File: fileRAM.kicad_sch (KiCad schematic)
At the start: 13 parts

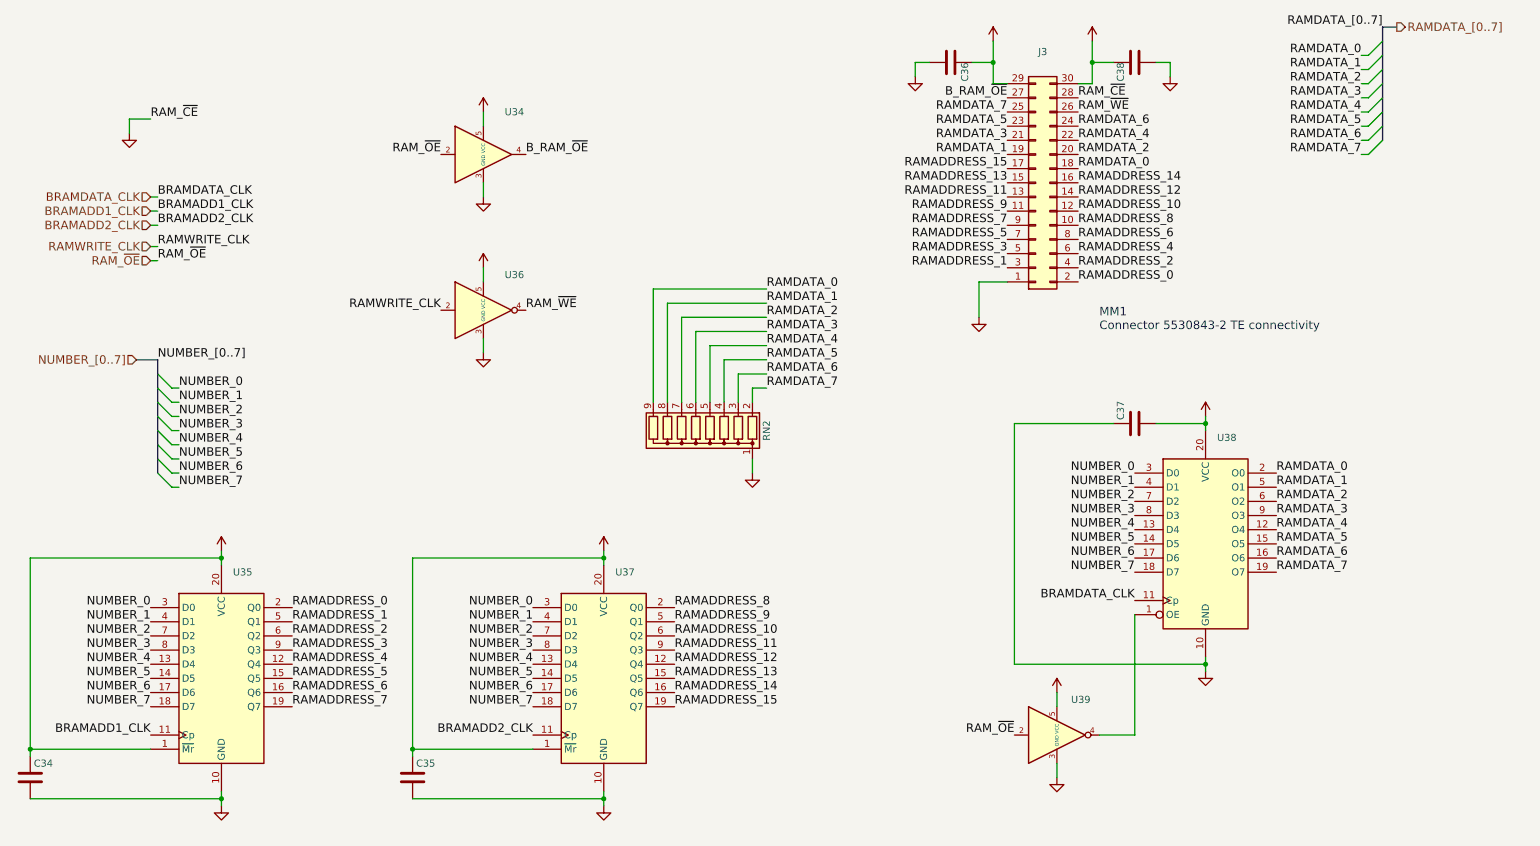
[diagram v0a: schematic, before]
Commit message: Updating descriptions
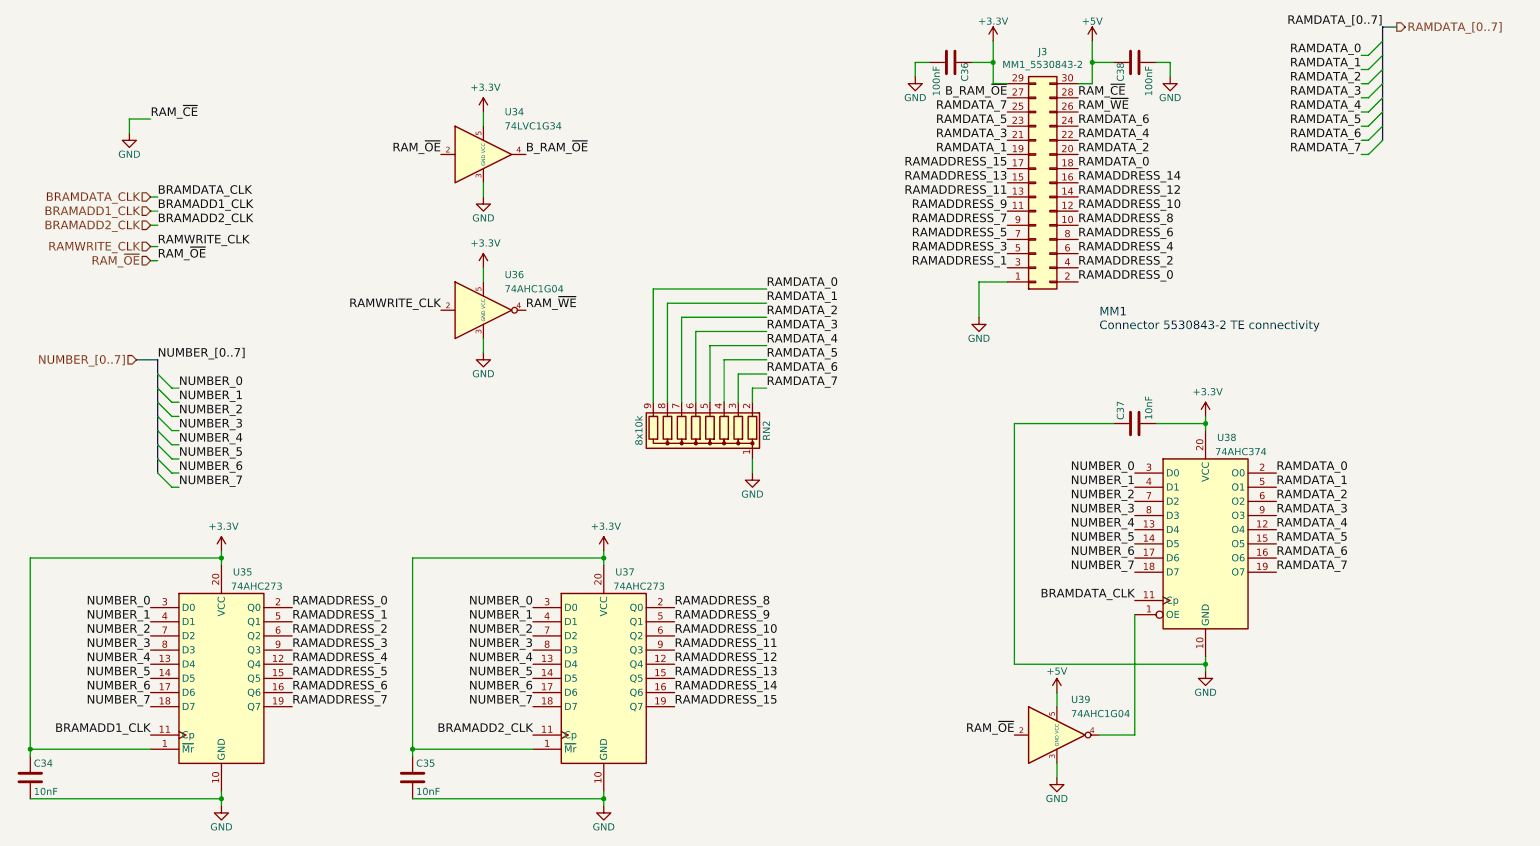
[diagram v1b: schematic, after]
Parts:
- C34, C35, C37: value (none) -> 10nF; footprint (none) -> Capacitor_SMD:C_0805_2012Metric
- C36, C38: value (none) -> 100nF; footprint (none) -> Capacitor_SMD:C_0805_2012Metric
- J3: value (none) -> MM1_5530843-2; footprint (none) -> TE5530843-2:TE_5530843-2
- RN2: value (none) -> 8x10k; footprint (none) -> Resistor_THT:R_Array_SIP9
- U34: value (none) -> 74LVC1G34; footprint (none) -> Package_TO_SOT_SMD:SOT-23-5
- U35, U37: value (none) -> 74AHC273; footprint (none) -> Package_SO:SOIC-20W_7.5x12.8mm_P1.27mm
- U36, U39: value (none) -> 74AHC1G04; footprint (none) -> Package_TO_SOT_SMD:SOT-23-5
- U38: value (none) -> 74AHC374; footprint (none) -> Package_SO:SOIC-20W_7.5x12.8mm_P1.27mm

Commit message: Finally remove clock sync, big improvement for the "if" instruction check (faster tps, less gates)
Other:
- note added: "RAM_~{CE}"
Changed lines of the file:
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@@
   (junction (at 16.51 151.13) (diameter 0) (color 0 0 0 0)
   )
+  (junction (at 220.98 34.29) (diameter 0) (color 0 0 0 0)
+  )
   (junction (at 207.01 27.94) (diameter 0) (color 0 0 0 0)
   )
@@
     (stroke (width 0) (type default) (color 0 0 0 0))
   )
-  (wire (pts (xy 38.1 38.1) (xy 34.29 38.1))
-    (stroke (width 0) (type default) (color 0 0 0 0))
-  )
   (bus (pts (xy 39.37 91.44) (xy 39.37 93.98))
     (stroke (width 0) (type default) (color 0 0 0 0))
@@
     (stroke (width 0) (type default) (color 0 0 0 0))
   )
+  (wire (pts (xy 204.47 34.29) (xy 220.98 34.29))
+    (stroke (width 0) (type default) (color 0 0 0 0))
+  )
   (wire (pts (xy 41.91 104.14) (xy 43.18 104.14))
     (stroke (width 0) (type default) (color 0 0 0 0))
   )
-  (wire (pts (xy 34.29 38.1) (xy 34.29 40.64))
-    (stroke (width 0) (type default) (color 0 0 0 0))
-  )
   (bus (pts (xy 39.37 93.98) (xy 39.37 96.52))
     (stroke (width 0) (type default) (color 0 0 0 0))
@@
     (stroke (width 0) (type default) (color 0 0 0 0))
   )
-  (wire (pts (xy 220.98 27.94) (xy 220.98 30.48))
+  (wire (pts (xy 220.98 27.94) (xy 220.98 34.29))
     (stroke (width 0) (type default) (color 0 0 0 0))
   )
@@
     (stroke (width 0) (type default) (color 0 0 0 0))
   )
+  (wire (pts (xy 220.98 34.29) (xy 220.98 35.56))
+    (stroke (width 0) (type default) (color 0 0 0 0))
+  )
   (wire (pts (xy 143.51 83.82) (xy 143.51 88.9))
     (stroke (width 0) (type default) (color 0 0 0 0))
@@
     (effects (font (size 1.524 1.524)) (justify left bottom))
   )
+  (text "RAM_~{CE}" (at 204.47 34.29 0)
+    (effects (font (size 1.524 1.524)) (justify left bottom))
+  )
   (label "RAMDATA_4" (at 148.59 78.74 0)
     (effects (font (size 1.524 1.524)) (justify left bottom))
@@
     (effects (font (size 1.524 1.524)) (justify left bottom))
   )
-  (label "RAM_~{CE}" (at 38.1 38.1 0)
-    (effects (font (size 1.524 1.524)) (justify left bottom))
-  )
   (label "RAMADDRESS_4" (at 204.47 62.23 0)
-    (effects (font (size 1.524 1.524)) (justify left bottom))
-  )
-  (label "RAM_~{CE}" (at 204.47 34.29 0)
     (effects (font (size 1.524 1.524)) (justify left bottom))
   )
@@
     (pin "1")
   )
-  (symbol (lib_id "Device:C") (at 181.61 27.94 270) (unit 1)
+  (symbol (lib_id "Device:C") (at 181.61 27.94 270) (mirror x) (unit 1)
     (in_bom yes) (on_board yes)
     (property "Reference" "C36" (id 0) (at 184.15 27.94 0)
       (effects (font (size 1.27 1.27)) (justify left))
     )
-    (property "Value" "100nF" (id 1) (at 179.07 28.575 0)
+    (property "Value" "100nF" (id 1) (at 179.07 27.305 0)
       (effects (font (size 1.27 1.27)) (justify left))
     )
-    (property "Footprint" "Capacitor_SMD:C_0805_2012Metric" (id 2) (at 177.8 28.9052 0)
+    (property "Footprint" "Capacitor_SMD:C_0805_2012Metric" (id 2) (at 177.8 26.9748 0)
       (effects (font (size 1.27 1.27)) hide)
     )
@@
     (pin "2")
   )
-  (symbol (lib_id "Device:C") (at 214.63 27.94 90) (mirror x) (unit 1)
+  (symbol (lib_id "Device:C") (at 214.63 27.94 90) (unit 1)
     (in_bom yes) (on_board yes)
     (property "Reference" "C38" (id 0) (at 212.09 27.94 0)
       (effects (font (size 1.27 1.27)) (justify left))
     )
-    (property "Value" "100nF" (id 1) (at 217.17 28.575 0)
+    (property "Value" "100nF" (id 1) (at 217.17 27.305 0)
       (effects (font (size 1.27 1.27)) (justify left))
     )
-    (property "Footprint" "Capacitor_SMD:C_0805_2012Metric" (id 2) (at 218.44 28.9052 0)
+    (property "Footprint" "Capacitor_SMD:C_0805_2012Metric" (id 2) (at 218.44 26.9748 0)
       (effects (font (size 1.27 1.27)) hide)
     )
@@
     (pin "2")
   )
-  (symbol (lib_id "power:GND") (at 220.98 30.48 0) (unit 1)
+  (symbol (lib_id "power:GND") (at 220.98 35.56 0) (unit 1)
     (in_bom yes) (on_board yes)
-    (property "Reference" "#PWR085" (id 0) (at 220.98 36.83 0)
-      (effects (font (size 1.27 1.27)) hide)
-    )
-    (property "Value" "GND" (id 1) (at 220.98 34.29 0))
-    (property "Footprint" "" (id 2) (at 220.98 30.48 0)
-      (effects (font (size 1.27 1.27)) hide)
-    )
-    (property "Datasheet" "" (id 3) (at 220.98 30.48 0)
+    (property "Reference" "#PWR085" (id 0) (at 220.98 41.91 0)
+      (effects (font (size 1.27 1.27)) hide)
+    )
+    (property "Value" "GND" (id 1) (at 220.98 39.37 0))
+    (property "Footprint" "" (id 2) (at 220.98 35.56 0)
+      (effects (font (size 1.27 1.27)) hide)
+    )
+    (property "Datasheet" "" (id 3) (at 220.98 35.56 0)
       (effects (font (size 1.27 1.27)) hide)
     )
@@
       (effects (font (size 1.27 1.27)) hide)
     )
-    (pin "1")
-  )
-  (symbol (lib_id "power:GND") (at 34.29 40.64 0) (unit 1)
-    (in_bom yes) (on_board yes)
-    (property "Reference" "#PWR087" (id 0) (at 34.29 46.99 0)
-      (effects (font (size 1.27 1.27)) hide)
-    )
-    (property "Value" "GND" (id 1) (at 34.29 44.45 0))
-    (property "Footprint" "" (id 2) (at 34.29 40.64 0)
-      (effects (font (size 1.27 1.27)) hide)
-    )
-    (property "Datasheet" "" (id 3) (at 34.29 40.64 0)
-      (effects (font (size 1.27 1.27)) hide)
-    )
